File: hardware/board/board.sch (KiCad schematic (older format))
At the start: 51 parts, among them J1 Eurorack Power, Q1 MMBT3904, U1 ATSAMD21G18A-AUT, U2 LM7805, U3 AP2112K-3.3, U4 LM4040DBZ-10, U5 TL072, U6 MCP6001-OT, U7 74AHCT1G125, U8 GD25Q64C

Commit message: Use unused op amp to level shift and buffer gate output
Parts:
- removed U3: AP2112K-3.3, Package_TO_SOT_SMD:SOT-23-5, symbol Regulator_Linear:AP2112K-3.3
- removed U7: 74AHCT1G125, Package_TO_SOT_SMD:SOT-23-5, symbol 74xGxx:74AHCT1G125
- added U?: LM1117-3.3, symbol Regulator_Linear:LM1117-3.3
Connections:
- wire segments 62 -> 61
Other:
- moved on the sheet: R11, U5B
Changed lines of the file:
@@
 Comment4 ""
 $EndDescr
-$Comp
-L Regulator_Linear:AP2112K-3.3 U3
-U 1 1 5E462447
-P 2850 1950
-F 0 "U3" H 2850 2292 50  0000 C CNN
-F 1 "AP2112K-3.3" H 2850 2201 50  0000 C CNN
-F 2 "Package_TO_SOT_SMD:SOT-23-5" H 2850 2275 50  0001 C CNN
-F 3 "https://www.diodes.com/assets/Datasheets/AP2112.pdf" H 2850 2050 50  0001 C CNN
-F 4 "AP2112K-3.3TRG1" H 2850 1950 50  0001 C CNN "mpn"
-	1    2850 1950
-	1    0    0    -1
-$EndComp
-$Comp
-L 74xGxx:74AHCT1G125 U7
-U 1 1 5E463A4D
-P 8200 1250
-F 0 "U7" H 8050 1400 50  0000 C CNN
-F 1 "74AHCT1G125" H 8600 1150 50  0000 C CNN
-F 2 "Package_TO_SOT_SMD:SOT-23-5" H 8200 1250 50  0001 C CNN
-F 3 "http://www.ti.com/lit/sg/scyt129e/scyt129e.pdf" H 8200 1250 50  0001 C CNN
-F 4 "SN74AHCT1G125DBVR" H 8200 1250 50  0001 C CNN "mpn"
-	1    8200 1250
-	1    0    0    -1
-$EndComp
 Wire Wire Line
 	2400 1250 2850 1250
@@
 Wire Wire Line
 	2550 1950 2550 1850
-Connection ~ 2550 1850
 $Comp
 L power:+12V #PWR0103
@@
 Text Notes 6000 1400 0    50   ~ 0
 Gain = -6.9\nVout = -11 to +11
-Text GLabel 7900 1250 0    50   Input ~ 0
+Text GLabel 8050 1150 0    50   Input ~ 0
 D0
-Text GLabel 8750 1250 2    50   Input ~ 0
+Text GLabel 8950 1250 2    50   Input ~ 0
 GATE_OUT
-$Comp
-L power:GND #PWR0121
-U 1 1 5E4A2C78
-P 8200 1050
-F 0 "#PWR0121" H 8200 800 50  0001 C CNN
-F 1 "GND" H 8205 877 50  0000 C CNN
-F 2 "" H 8200 1050 50  0001 C CNN
-F 3 "" H 8200 1050 50  0001 C CNN
-	1    8200 1050
-	-1   0    0    1
-$EndComp
-$Comp
-L power:GND #PWR0122
-U 1 1 5E4A319B
-P 8250 1300
-F 0 "#PWR0122" H 8250 1050 50  0001 C CNN
-F 1 "GND" H 8255 1127 50  0000 C CNN
-F 2 "" H 8250 1300 50  0001 C CNN
-F 3 "" H 8250 1300 50  0001 C CNN
-	1    8250 1300
-	1    0    0    -1
-$EndComp
-$Comp
-L power:+5V #PWR0123
-U 1 1 5E4A4329
-P 8250 1200
-F 0 "#PWR0123" H 8250 1050 50  0001 C CNN
-F 1 "+5V" H 8265 1373 50  0000 C CNN
-F 2 "" H 8250 1200 50  0001 C CNN
-F 3 "" H 8250 1200 50  0001 C CNN
-	1    8250 1200
-	1    0    0    -1
-$EndComp
 $Comp
 L Device:R_US R8
@@
 L Device:R_US R11
 U 1 1 5E5547AE
-P 8600 1250
-F 0 "R11" V 8393 1250 50  0000 C CNN
-F 1 "1k" V 8484 1250 50  0000 C CNN
-F 2 "Resistor_SMD:R_0603_1608Metric_Pad1.05x0.95mm_HandSolder" V 8530 1250 50  0001 C CNN
-F 3 "~" H 8600 1250 50  0001 C CNN
-F 4 "MF-RES-0603-1K" H 8600 1250 50  0001 C CNN "mpn"
-	1    8600 1250
+P 8800 1250
+F 0 "R11" V 8593 1250 50  0000 C CNN
+F 1 "1k" V 8684 1250 50  0000 C CNN
+F 2 "Resistor_SMD:R_0603_1608Metric_Pad1.05x0.95mm_HandSolder" V 8730 1250 50  0001 C CNN
+F 3 "~" H 8800 1250 50  0001 C CNN
+F 4 "MF-RES-0603-1K" H 8800 1250 50  0001 C CNN "mpn"
+	1    8800 1250
 	0    1    1    0
 $EndComp
@@
 L Amplifier_Operational:TL072 U5
 U 2 1 5E6B95A0
-P 6400 2200
-F 0 "U5" H 6400 2567 50  0000 C CNN
-F 1 "TL072" H 6400 2476 50  0000 C CNN
-F 2 "Package_SO:TSSOP-8_4.4x3mm_P0.65mm" H 6400 2200 50  0001 C CNN
-F 3 "http://www.ti.com/lit/ds/symlink/tl072.pdf" H 6400 2200 50  0001 C CNN
-F 4 "TL072CPWR" H 6400 2200 50  0001 C CNN "mpn"
-	2    6400 2200
-	1    0    0    -1
-$EndComp
-$Comp
-L power:GND #PWR0149
-U 1 1 5E6C8D4E
-P 6100 2100
-F 0 "#PWR0149" H 6100 1850 50  0001 C CNN
-F 1 "GND" V 6105 1972 50  0000 R CNN
-F 2 "" H 6100 2100 50  0001 C CNN
-F 3 "" H 6100 2100 50  0001 C CNN
-	1    6100 2100
-	0    1    1    0
-$EndComp
-Wire Wire Line
-	6100 2300 6100 2450
-Wire Wire Line
-	6100 2450 6700 2450
+P 8350 1250
+F 0 "U5" H 8350 1617 50  0000 C CNN
+F 1 "TL072" H 8350 1526 50  0000 C CNN
+F 2 "Package_SO:TSSOP-8_4.4x3mm_P0.65mm" H 8350 1250 50  0001 C CNN
+F 3 "http://www.ti.com/lit/ds/symlink/tl072.pdf" H 8350 1250 50  0001 C CNN
+F 4 "TL072CPWR" H 8350 1250 50  0001 C CNN "mpn"
+	2    8350 1250
+	1    0    0    -1
+$EndComp
 Wire Wire Line
 	6700 2450 6700 2200
-Text Notes 6400 2400 0    50   ~ 0
+Text Notes 8375 1450 0    50   ~ 0
 unused
 $Comp
@@
 Text Notes 3550 4200 0    50   ~ 0
 Grounded for v5+
+$Comp
+L Regulator_Linear:LM1117-3.3 U?
+U 1 1 61112C9A
+P 2850 1850
+F 0 "U?" H 2850 2092 50  0000 C CNN
+F 1 "LM1117-3.3" H 2850 2001 50  0000 C CNN
+F 2 "" H 2850 1850 50  0001 C CNN
+F 3 "http://www.ti.com/lit/ds/symlink/lm1117.pdf" H 2850 1850 50  0001 C CNN
+	1    2850 1850
+	1    0    0    -1
+$EndComp
+Connection ~ 2550 1850
+Wire Wire Line
+	2850 2150 2850 2250
 $EndSCHEMATC

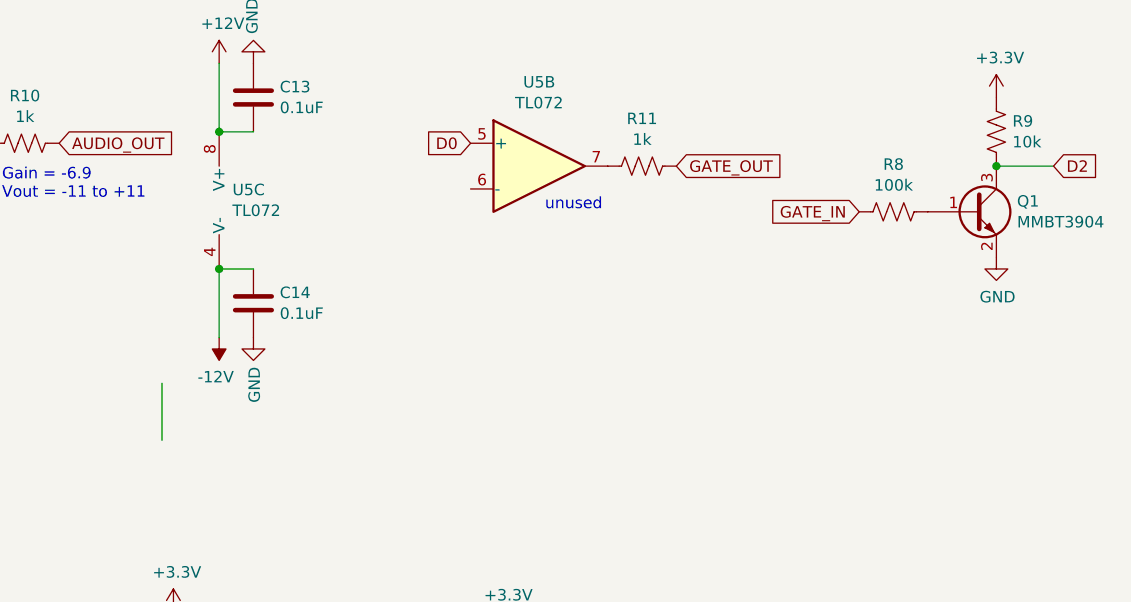
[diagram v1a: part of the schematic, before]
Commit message: Diode to protect transistor
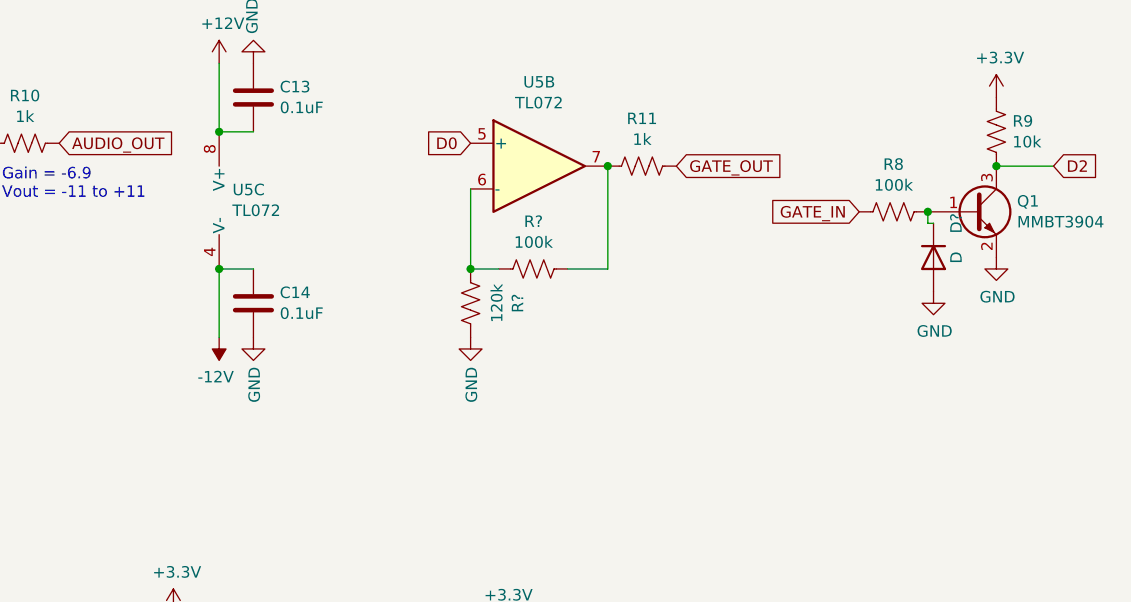
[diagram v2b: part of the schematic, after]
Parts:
- added D?: D, Diode_SMD:D_SOD-123, symbol Device:D
- added R?: 100k, Resistor_SMD:R_0603_1608Metric_Pad1.05x0.95mm_HandSolder, symbol Device:R_US
- added R?: 120k, Resistor_SMD:R_0603_1608Metric_Pad1.05x0.95mm_HandSolder, symbol Device:R_US
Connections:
- wire segments 61 -> 66
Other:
- note removed: "unused"
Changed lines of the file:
@@
 	1    0    0    -1
 $EndComp
-Wire Wire Line
-	6700 2450 6700 2200
-Text Notes 8375 1450 0    50   ~ 0
-unused
 $Comp
 L board:GD25Q64C U8
@@
 Wire Wire Line
 	2850 2150 2850 2250
+$Comp
+L Device:R_US R?
+U 1 1 61117147
+P 8325 1700
+F 0 "R?" V 8118 1700 50  0000 C CNN
+F 1 "100k" V 8209 1700 50  0000 C CNN
+F 2 "Resistor_SMD:R_0603_1608Metric_Pad1.05x0.95mm_HandSolder" V 8255 1700 50  0001 C CNN
+F 3 "~" H 8325 1700 50  0001 C CNN
+F 4 "MF-RES-0603-1K" H 8325 1700 50  0001 C CNN "mpn"
+	1    8325 1700
+	0    1    1    0
+$EndComp
+$Comp
+L Device:R_US R?
+U 1 1 61117843
+P 8050 1850
+F 0 "R?" V 7843 1850 50  0000 C CNN
+F 1 "120k" V 7934 1850 50  0000 C CNN
+F 2 "Resistor_SMD:R_0603_1608Metric_Pad1.05x0.95mm_HandSolder" V 7980 1850 50  0001 C CNN
+F 3 "~" H 8050 1850 50  0001 C CNN
+F 4 "MF-RES-0603-1K" H 8050 1850 50  0001 C CNN "mpn"
+	1    8050 1850
+	-1   0    0    1
+$EndComp
+Wire Wire Line
+	8050 1350 8050 1700
+Wire Wire Line
+	8050 1700 8175 1700
+Connection ~ 8050 1700
+Wire Wire Line
+	8475 1700 8650 1700
+Wire Wire Line
+	8650 1700 8650 1250
+Connection ~ 8650 1250
+$Comp
+L power:GND #PWR?
+U 1 1 6111B89B
+P 8050 2000
+F 0 "#PWR?" H 8050 1750 50  0001 C CNN
+F 1 "GND" V 8055 1872 50  0000 R CNN
+F 2 "" H 8050 2000 50  0001 C CNN
+F 3 "" H 8050 2000 50  0001 C CNN
+	1    8050 2000
+	1    0    0    -1
+$EndComp
+$Comp
+L Device:D D?
+U 1 1 6111BB60
+P 10075 1650
+F 0 "D?" H 9925 1750 50  0000 C CNN
+F 1 "D" H 10075 1750 50  0000 C CNN
+F 2 "Diode_SMD:D_SOD-123" H 10075 1650 50  0001 C CNN
+F 3 "~" H 10075 1650 50  0001 C CNN
+F 4 "MF-DIO-SOD123-1N4148" H 10075 1650 50  0001 C CNN "mpn"
+	1    10075 1650
+	0    1    1    0
+$EndComp
+Wire Wire Line
+	10050 1450 10050 1500
+Wire Wire Line
+	10050 1500 10075 1500
+Connection ~ 10050 1450
+$Comp
+L power:GND #PWR?
+U 1 1 6111E3A7
+P 10075 1800
+F 0 "#PWR?" H 10075 1550 50  0001 C CNN
+F 1 "GND" H 10080 1627 50  0000 C CNN
+F 2 "" H 10075 1800 50  0001 C CNN
+F 3 "" H 10075 1800 50  0001 C CNN
+	1    10075 1800
+	1    0    0    -1
+$EndComp
 $EndSCHEMATC
